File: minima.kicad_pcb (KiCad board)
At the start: 2 copper layers, 90 x 60 mm, 37 parts, among them J1 output, J2 input, J3 powersupply, U1 LM1875

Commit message: Version 1.0b
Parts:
- removed the C6 at (117.0, 55.3)
- removed the R3 at (136.7, 66.1)
- removed the R5 at (176.6, 50.3)
- added C3: 15p, Capacitor_THT:C_Disc_D3.8mm_W2.6mm_P2.50mm, F.Cu at (123.3, 59.8)
- added LOGO1: OSHW Logo, Symbol:OSHW-Logo2_7.3x6mm_SilkScreen, F.Cu at (119.6, 100.7)
- added R1: 499, Resistor_THT:R_Axial_DIN0207_L6.3mm_D2.5mm_P10.16mm_Horizontal, F.Cu at (136.7, 66.1)
- added R8: 4.7, Resistor_THT:R_Axial_DIN0411_L9.9mm_D3.6mm_P15.24mm_Horizontal, F.Cu at (173.5, 50.2)
- C1: value 15p -> 470u; footprint Capacitor_THT:C_Disc_D3.4mm_W2.1mm_P2.50mm -> Capacitor_THT:CP_Radial_D8.0mm_P3.50mm
- J1: value output -> input; footprint Connector_Phoenix_MC:PhoenixContact_MCV_1,5_2-G-3.5_1x02_P3.50mm_Vertical -> TerminalBlock_Phoenix:TerminalBlock_Phoenix_PT-1,5-3-3.5-H_1x03_P3.50mm_Horizontal
- J2: value input -> powersupply; footprint TerminalBlock_Phoenix:TerminalBlock_Phoenix_MPT-0,5-4-2.54_1x04_P2.54mm_Horizontal -> TerminalBlock_Phoenix:TerminalBlock_Phoenix_MKDS-3-3-5.08_1x03_P5.08mm_Horizontal
- J3: value powersupply -> output; footprint Connector_Phoenix_MC:PhoenixContact_MCV_1,5_3-G-3.5_1x03_P3.50mm_Vertical -> TerminalBlock_Phoenix:TerminalBlock_Phoenix_MKDS-3-2-5.08_1x02_P5.08mm_Horizontal
- LOGO2: value OSHW Logo -> Kicad_Logo; footprint Symbol:OSHW-Logo2_14.6x12mm_SilkScreen -> Symbol:KiCad-Logo_5mm_Copper; moved to B.Cu
- MK1, MK2, MK3, MK4: footprint MountingHole:MountingHole_3.2mm_M3_ISO7380 -> MountingHole:MountingHole_3.2mm_M3_ISO7380_Pad
- moved MK2 76.0 mm to (182.6, 51.7)
- moved MK3 76.0 mm to (108.6, 51.7)
- moved J1 63.8 mm to (108.2, 88.3)
- moved R12 38.8 mm to (136.7, 69.9), turned to 180 degrees
- moved J2 38.5 mm to (140.6, 99.7)
- moved D1 30.0 mm to (182.4, 61.7), turned to 270 degrees
- moved J3 28.6 mm to (169.1, 99.7)
- moved C5 19.9 mm to (173.5, 72.4), turned to 180 degrees
- moved C1 15.3 mm to (108.1, 61.0)
- moved C11 10.5 mm to (131.6, 88.3), turned to 90 degrees
- moved C13 9.88 mm to (111.9, 73.1)
- moved C12 7.96 mm to (111.9, 79.4)
- moved D2 4.58 mm to (182.4, 78.2), turned to 270 degrees
- moved R9 4.34 mm to (106.8, 82.6)
- moved R10 4.26 mm to (106.8, 76.3)
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- renumbered C7 to C4, C3 to C5, C4 to C6, C8 to C7, C5 to C8, R6 to R2, R1 to R3, R7 to R5, R8 to R6, R2 to R7
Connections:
- C1 pad 1: /Input amplifier/sgnd -> Net-(C1-Pad1)
- C1 pad 2: Net-(C1-Pad2) -> /Power amplifier/inp
- C2 pad 2: /Power amplifier/inp -> /Input amplifier/sgnd
- C4 pad 1: Net-(C3-Pad2) -> Net-(C4-Pad1)
- C5 pad 2: Net-(C3-Pad2) -> Net-(C4-Pad1)
- D1 pad 2: Net-(C3-Pad2) -> /Power amplifier/spkhot
- D2 pad 1: Net-(C3-Pad2) -> /Power amplifier/spkhot
- J1 pad 1: /Power amplifier/spkhot -> /Input amplifier/inp
- J2 pad 1: /Input amplifier/inp -> VEE
- J2 pad 3: /Input amplifier/sgnd -> VCC
- J3 pad 1: VCC -> GNDPWR
- J3 pad 2: VEE -> /Power amplifier/spkhot
- L1 pad 1: Net-(C3-Pad2) -> Net-(C4-Pad1)
- R2 pad 2: Net-(C6-Pad1) -> Net-(C2-Pad1)
- R3 pad 2: Net-(C1-Pad2) -> Net-(C3-Pad2)
- R5 pad 1: Net-(C3-Pad2) -> Net-(C4-Pad1)
- U1 pad 4: Net-(C3-Pad2) -> Net-(C4-Pad1)
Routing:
- net GNDPWR: track 0.00 -> 103.8 mm
- net /Input amplifier/sgnd: track 0.00 -> 78.3 mm
- net /Power amplifier/spkhot: track 0.00 -> 62.5 mm
- net Net-(C4-Pad1): track 0.00 -> 60.9 mm
- net VEE: track 0.00 -> 51.1 mm
- net VCC: track 0.00 -> 33.1 mm
- net Net-(C1-Pad1): track 0.00 -> 20.5 mm
- net /Power amplifier/inp: track 0.00 -> 18.7 mm
- net Net-(R1-Pad1): track 0.00 -> 14.8 mm
- net Net-(R2-Pad1): track 0.00 -> 13.6 mm
- net Net-(C12-Pad1): track 0.00 -> 12.8 mm
- net /Input amplifier/inp: track 0.00 -> 11.9 mm
- net Net-(C2-Pad1): track 0.00 -> 11.4 mm
- net Net-(C5-Pad1): track 0.00 -> 4.38 mm
- net Net-(C4-Pad2): track 0.00 -> 3.45 mm
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- added copper zone on B.Cu, net Net-(C4-Pad1)
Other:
- board size 90 x 60 mm -> 86 x 60 mm
- board text added: "+|G|SG"
- board text added: "-|G|+"
- board text added: "G|+"

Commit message: Release Version 1.0
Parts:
- R12: footprint Resistor_THT:R_Axial_DIN0309_L9.0mm_D3.2mm_P12.70mm_Horizontal -> Resistor_THT:R_Axial_DIN0207_L6.3mm_D2.5mm_P10.16mm_Horizontal
- R4, R5: value 15k -> 7k5
- moved LOGO2 12.3 mm to (131.5, 98.0)
- moved LOGO1 4.21 mm to (120.8, 96.5)
- renumbered LOGO2 to LOGO1, LOGO1 to LOGO2
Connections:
- D1 pad 2: /Power amplifier/spkhot -> Net-(C4-Pad1)
- D2 pad 1: /Power amplifier/spkhot -> Net-(C4-Pad1)
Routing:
- net Net-(C4-Pad1): track 60.9 -> 99.8 mm
- net VCC: track 33.1 -> 48.2 mm
- net /Power amplifier/spkhot: track 62.5 -> 52.6 mm
- net /Input amplifier/sgnd: track 78.3 -> 75.0 mm
- net GNDPWR: track 103.8 -> 102.3 mm
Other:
- board text added: "01.08.2018 1.0"
- board text added: "Minima V1.0"
- board text added: "Real-Time Consulting"

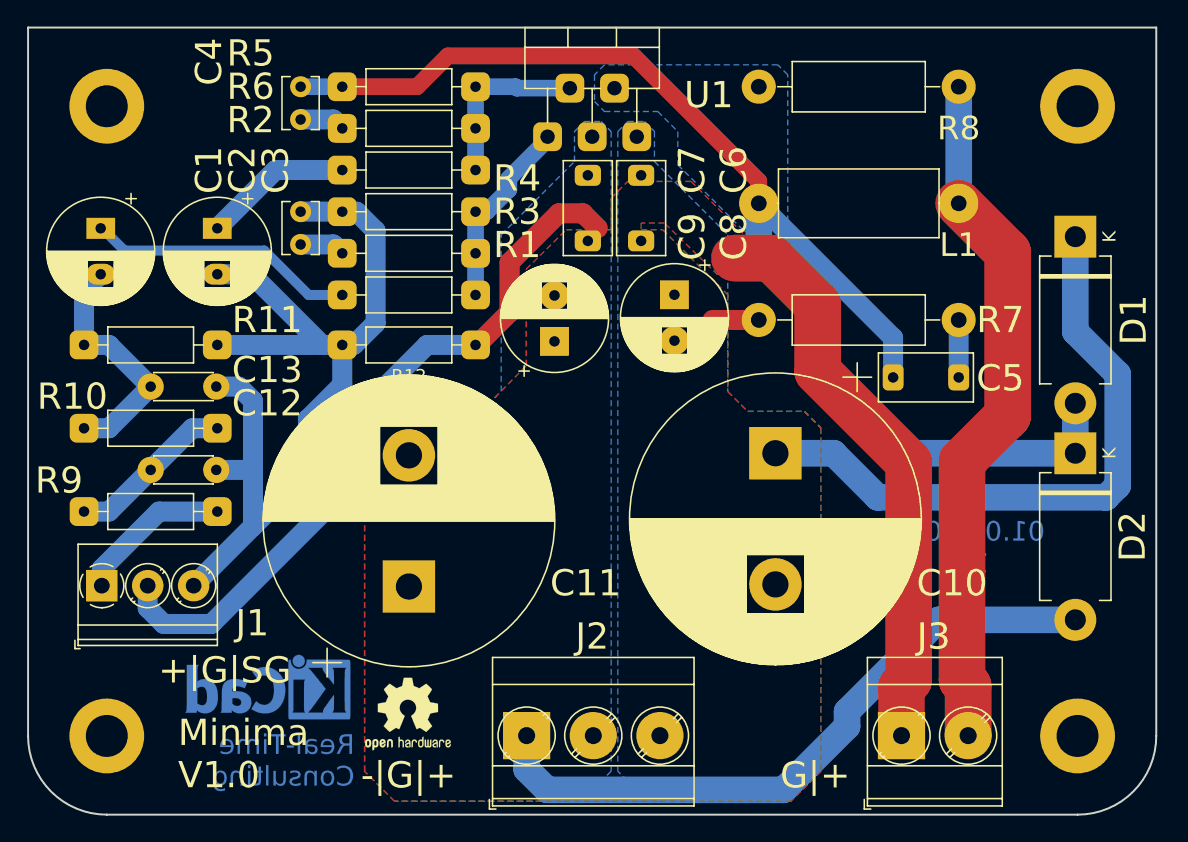
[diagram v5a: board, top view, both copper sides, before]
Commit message: Releasing version with distant psu caps.
Signed-off-by: Nenad Radulovic <nenad.b.radulovic@gmail.com>
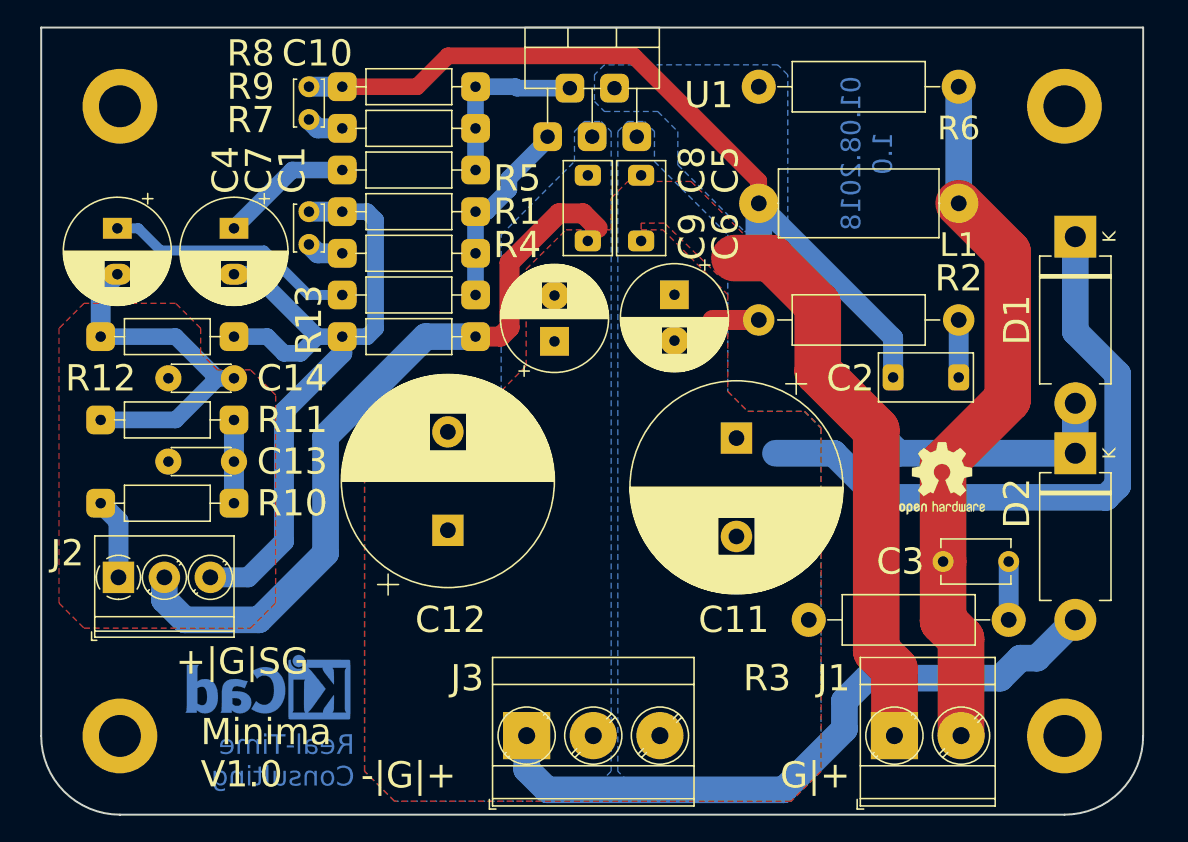
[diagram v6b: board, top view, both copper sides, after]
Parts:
- removed the C4 at (123.3, 50.2)
- removed the J3 at (169.1, 99.7)
- removed the R7 at (158.3, 68.0)
- added C1: 15p, Capacitor_THT:C_Disc_D3.4mm_W2.1mm_P2.50mm, F.Cu at (124.0, 59.8)
- added C12: 2m2, Capacitor_THT:CP_Radial_D16.0mm_P7.50mm, F.Cu at (134.6, 84.0)
- added J2: input, TerminalBlock_Phoenix:TerminalBlock_Phoenix_PT-1,5-3-3.5-H_1x03_P3.50mm_Horizontal, F.Cu at (109.5, 87.6)
- added R2: 4.7, Resistor_THT:R_Axial_DIN0411_L9.9mm_D3.6mm_P15.24mm_Horizontal, F.Cu at (158.3, 68.0)
- added R3: 10, Resistor_THT:R_Axial_DIN0411_L9.9mm_D3.6mm_P15.24mm_Horizontal, F.Cu at (162.1, 90.9)
- C10: value 4m7 -> 15p; footprint Capacitor_THT:CP_Radial_D22.0mm_P10.00mm_SnapIn -> Capacitor_THT:C_Disc_D3.4mm_W2.1mm_P2.50mm
- C11: value 4m7 -> 2m2; footprint Capacitor_THT:CP_Radial_D22.0mm_P10.00mm_SnapIn -> Capacitor_THT:CP_Radial_D16.0mm_P7.50mm
- C3: value 15p -> 100n; footprint Capacitor_THT:C_Disc_D3.8mm_W2.6mm_P2.50mm -> Capacitor_THT:C_Disc_D5.1mm_W3.2mm_P5.00mm
- J1: value input -> output; footprint TerminalBlock_Phoenix:TerminalBlock_Phoenix_PT-1,5-3-3.5-H_1x03_P3.50mm_Horizontal -> TerminalBlock_Phoenix:TerminalBlock_Phoenix_MKDS-3-2-5.08_1x02_P5.08mm_Horizontal
- moved J1 61.5 mm to (168.6, 99.7)
- moved C3 60.2 mm to (177.3, 86.4), turned to 180 degrees
- moved C10 45.2 mm to (124.0, 50.2)
- moved LOGO2 44.5 mm to (172.2, 80.1)
- moved C11 27.4 mm to (156.6, 77.0), turned to 270 degrees
- moved R10 11.4 mm to (118.3, 82.0), turned to 180 degrees
- moved C14 6.38 mm to (118.3, 72.5), turned to 180 degrees
- moved C13 6.38 mm to (118.3, 78.8), turned to 180 degrees
- moved R11 1.42 mm to (108.1, 75.6)
- moved R12 1.42 mm to (108.1, 69.3)
- moved C4 1.27 mm to (109.4, 61.0)
- moved C7 1.27 mm to (118.3, 61.0)
- moved MK1 1.00 mm to (109.6, 99.7)
- moved MK2 1.00 mm to (109.6, 51.7)
- moved MK3 1.00 mm to (181.6, 51.7)
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- renumbered C12 to C13, C13 to C14, C5 to C2, C1 to C4, C6 to C5, C8 to C6, C2 to C7, C7 to C8, J2 to J3, MK3 to MK2, MK2 to MK3, R3 to R1, R9 to R10, R10 to R11, R11 to R12, R12 to R13, R1 to R4, R4 to R5, R8 to R6, R2 to R7, R5 to R8, R6 to R9
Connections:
- C10 pad 1: VCC -> Net-(C10-Pad1)
- C10 pad 2: GNDPWR -> Net-(C10-Pad2)
- C11 pad 1: GNDPWR -> VCC
- C11 pad 2: VEE -> GNDPWR
- C2 pad 2: Net-(C4-Pad1) (its old number) -> Net-(C10-Pad1)
- C3 pad 1: /Input amplifier/sgnd -> Net-(C3-Pad1)
- C3 pad 2: Net-(C3-Pad2) -> /Power amplifier/spkhot
- D1 pad 2: Net-(C4-Pad1) (its old number) -> Net-(C10-Pad1)
- D2 pad 1: Net-(C4-Pad1) (its old number) -> Net-(C10-Pad1)
- J1 pad 1: /Input amplifier/inp -> GNDPWR
- J1 pad 2: GNDPWR -> /Power amplifier/spkhot
- L1 pad 1: Net-(C4-Pad1) (its old number) -> Net-(C10-Pad1)
- R1 pad 2: Net-(C3-Pad2) -> Net-(C1-Pad2)
- R6 pad 2: Net-(C4-Pad1) (its old number) -> Net-(C10-Pad1)
- R8 pad 1: Net-(C4-Pad1) (its old number) -> Net-(C10-Pad1)
- R9 pad 2: Net-(C4-Pad2) -> Net-(C10-Pad2)
- U1 pad 4: Net-(C4-Pad1) (its old number) -> Net-(C10-Pad1)
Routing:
- net Net-(C4-Pad1) (its old number): track 99.8 -> 0.00 mm
- net Net-(C10-Pad1): track 0.00 -> 99.2 mm
- net /Input amplifier/sgnd: track 75.0 -> 58.2 mm
- net /Power amplifier/inp: track 18.7 -> 27.0 mm
- net Net-(C13-Pad1): track 12.8 -> 6.35 mm
- net /Input amplifier/inp: track 11.9 -> 6.21 mm
- net Net-(C3-Pad1): track 0.00 -> 4.45 mm
- net Net-(C4-Pad2): track 3.45 -> 0.00 mm
- net Net-(C3-Pad2): track 3.45 -> 0.00 mm
- net Net-(C10-Pad2): track 0.00 -> 2.82 mm
- net Net-(C1-Pad2): track 0.00 -> 2.82 mm
- net Net-(C7-Pad1): track 11.4 -> 10.1 mm
- net Net-(C4-Pad1): track 20.5 -> 19.2 mm
- net GNDPWR: track 102.3 -> 103.4 mm
- net /Power amplifier/spkhot: track 52.6 -> 53.6 mm
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- added copper zone on F.Cu, net /Input amplifier/sgnd
- added copper zone on B.Cu, net Net-(C10-Pad1)
- removed copper zone on B.Cu, net Net-(C4-Pad1) (its old number)
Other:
- board size 86 x 60 mm -> 84 x 60 mm

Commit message: Relase v1.0
Corrected a few things on the PCB.
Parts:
- C14: value 1n -> 2n2
- R1, R10, R11, R12, R9: footprint Resistor_THT:R_Axial_DIN0207_L6.3mm_D2.5mm_P10.16mm_Horizontal -> Resistor_THT:R_Axial_DIN0207_L6.3mm_D2.5mm_P7.62mm_Horizontal
- moved C10 3.18 mm to (124.0, 53.4), turned to 0 degrees
- moved C1 3.17 mm to (124.0, 62.9), turned to 0 degrees
- moved R11 2.54 mm to (110.6, 75.6)
- moved R12 2.54 mm to (110.6, 69.3)
- moved J2 1.82 mm to (111.3, 87.6)
- moved LOGO2 1.80 mm to (171.0, 78.8)
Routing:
- net GNDPWR: track 103.4 -> 110.7 mm
- net /Power amplifier/inp: track 27.0 -> 21.9 mm
- net VEE: track 51.7 -> 56.0 mm
- net VCC: track 48.2 -> 52.3 mm
- net /Input amplifier/sgnd: track 58.2 -> 61.4 mm
- net Net-(C10-Pad1): track 99.2 -> 102.0 mm
